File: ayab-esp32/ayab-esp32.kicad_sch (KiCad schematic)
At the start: 13 parts

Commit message: review ZVD P-ch MOSFET and resistors
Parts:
- FID101, FID102, FID103: symbol Library:Fiducial -> ayab-lib:Fiducial
- H101, H102, H103, H104, H105, H106, H107, H108: symbol Library:MountingHole_Pad -> ayab-lib:MountingHole_Pad
- R101, R102: symbol Library:R_Small_US -> ayab-lib:R_Small_US
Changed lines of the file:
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@@
     (effects (font (size 1.27 1.27)) (justify left bottom))
   )
-  (symbol (lib_id "Library:Fiducial") (at 40.64 111.76 0) (unit 1)
+  (symbol (lib_id "ayab-lib:Fiducial") (at 40.64 111.76 0) (unit 1)
     (in_bom no) (on_board yes) (dnp no) (fields_autoplaced)
     (property "Reference" "FID101" (at 43.18 110.49 0)
@@
     )
   )
-  (symbol (lib_id "Library:MountingHole_Pad") (at 71.12 123.19 0) (unit 1)
+  (symbol (lib_id "ayab-lib:MountingHole_Pad") (at 71.12 123.19 0) (unit 1)
     (in_bom no) (on_board yes) (dnp no) (fields_autoplaced)
     (property "Reference" "H107" (at 73.66 120.65 0)
@@
     )
   )
-  (symbol (lib_id "Library:R_Small_US") (at 68.58 81.28 90) (unit 1)
+  (symbol (lib_id "ayab-lib:R_Small_US") (at 68.58 81.28 90) (unit 1)
     (in_bom yes) (on_board yes) (dnp no)
     (property "Reference" "R101" (at 64.77 78.74 90)
@@
     )
   )
-  (symbol (lib_id "Library:Fiducial") (at 55.88 111.76 0) (unit 1)
+  (symbol (lib_id "ayab-lib:Fiducial") (at 55.88 111.76 0) (unit 1)
     (in_bom no) (on_board yes) (dnp no) (fields_autoplaced)
     (property "Reference" "FID102" (at 58.42 110.49 0)
@@
     )
   )
-  (symbol (lib_id "Library:MountingHole_Pad") (at 40.64 123.19 0) (unit 1)
+  (symbol (lib_id "ayab-lib:MountingHole_Pad") (at 40.64 123.19 0) (unit 1)
     (in_bom no) (on_board yes) (dnp no) (fields_autoplaced)
     (property "Reference" "H101" (at 43.18 120.65 0)
@@
     )
   )
-  (symbol (lib_id "Library:MountingHole_Pad") (at 50.8 123.19 0) (unit 1)
+  (symbol (lib_id "ayab-lib:MountingHole_Pad") (at 50.8 123.19 0) (unit 1)
     (in_bom no) (on_board yes) (dnp no) (fields_autoplaced)
     (property "Reference" "H103" (at 53.34 120.65 0)
@@
     )
   )
-  (symbol (lib_id "Library:MountingHole_Pad") (at 60.96 134.62 0) (unit 1)
+  (symbol (lib_id "ayab-lib:MountingHole_Pad") (at 60.96 134.62 0) (unit 1)
     (in_bom no) (on_board yes) (dnp no) (fields_autoplaced)
     (property "Reference" "H106" (at 63.5 132.08 0)
@@
     )
   )
-  (symbol (lib_id "Library:Fiducial") (at 71.12 111.76 0) (unit 1)
+  (symbol (lib_id "ayab-lib:Fiducial") (at 71.12 111.76 0) (unit 1)
     (in_bom no) (on_board yes) (dnp no) (fields_autoplaced)
     (property "Reference" "FID103" (at 73.66 110.49 0)
@@
     )
   )
-  (symbol (lib_id "Library:R_Small_US") (at 68.58 86.36 90) (unit 1)
+  (symbol (lib_id "ayab-lib:R_Small_US") (at 68.58 86.36 90) (unit 1)
     (in_bom yes) (on_board yes) (dnp no)
     (property "Reference" "R102" (at 64.77 83.82 90)
@@
     )
   )
-  (symbol (lib_id "Library:MountingHole_Pad") (at 71.12 134.62 0) (unit 1)
+  (symbol (lib_id "ayab-lib:MountingHole_Pad") (at 71.12 134.62 0) (unit 1)
     (in_bom no) (on_board yes) (dnp no) (fields_autoplaced)
     (property "Reference" "H108" (at 73.66 132.08 0)
@@
     )
   )
-  (symbol (lib_id "Library:MountingHole_Pad") (at 50.8 134.62 0) (unit 1)
+  (symbol (lib_id "ayab-lib:MountingHole_Pad") (at 50.8 134.62 0) (unit 1)
     (in_bom no) (on_board yes) (dnp no) (fields_autoplaced)
     (property "Reference" "H104" (at 53.34 132.08 0)
@@
     )
   )
-  (symbol (lib_id "Library:MountingHole_Pad") (at 40.64 134.62 0) (unit 1)
+  (symbol (lib_id "ayab-lib:MountingHole_Pad") (at 40.64 134.62 0) (unit 1)
     (in_bom no) (on_board yes) (dnp no) (fields_autoplaced)
     (property "Reference" "H102" (at 43.18 132.08 0)
@@
     )
   )
-  (symbol (lib_id "Library:MountingHole_Pad") (at 60.96 123.19 0) (unit 1)
+  (symbol (lib_id "ayab-lib:MountingHole_Pad") (at 60.96 123.19 0) (unit 1)
     (in_bom no) (on_board yes) (dnp no) (fields_autoplaced)
     (property "Reference" "H105" (at 63.5 120.65 0)

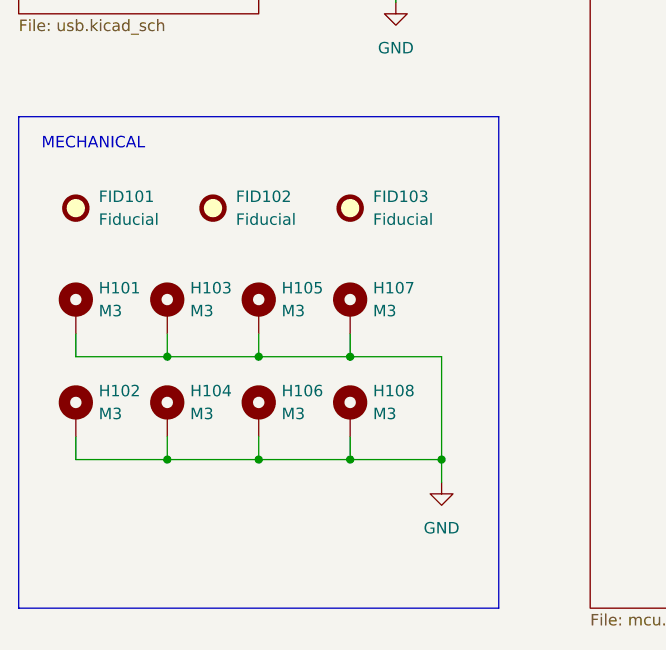
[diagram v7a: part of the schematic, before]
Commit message: first draft layout DRC clean
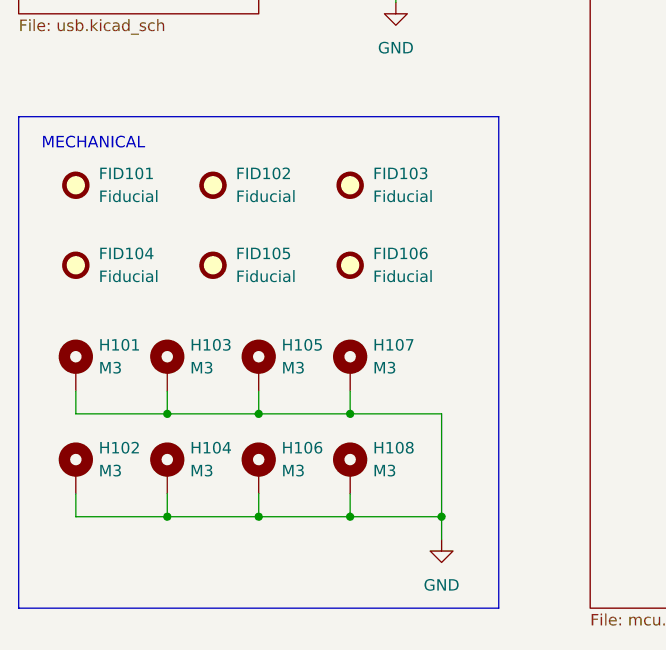
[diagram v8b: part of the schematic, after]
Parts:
- added FID104, FID105, FID106: Fiducial, Fiducial:Fiducial_1mm_Mask2mm, symbol ayab-lib:Fiducial
- FID101, FID102, FID103: footprint Fiducial:Fiducial_0.5mm_Mask1.5mm -> Fiducial:Fiducial_1mm_Mask2mm
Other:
- moved on the sheet: FID101, FID102, FID103, H101, H102, H103, H104, H105, H106, H107, H108
